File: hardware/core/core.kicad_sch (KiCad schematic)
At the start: 82 parts, among them J1 9V_IN, J2 MIDI IN, J3 MIDI OUT 1, J4 MIDI OUT 2, J5 MIDI OUT 3, J6 MIDI OUT 4, J7 LCD, J8 USB_C_Receptacle_USB2.0_16P, SW1 FS, SW10 BOOT, SW2 FS, SW3 FS, SW4 FS, SW5 FS, SW6 FS, SW7 FS, SW8 FS, SW9 RESET, U1 LM2596S-5, U2 6N137, U3 ESP32-S3-WROOM-1, U4 LD1117-3.3V-SOT223, U5 USBLC6-2SC6

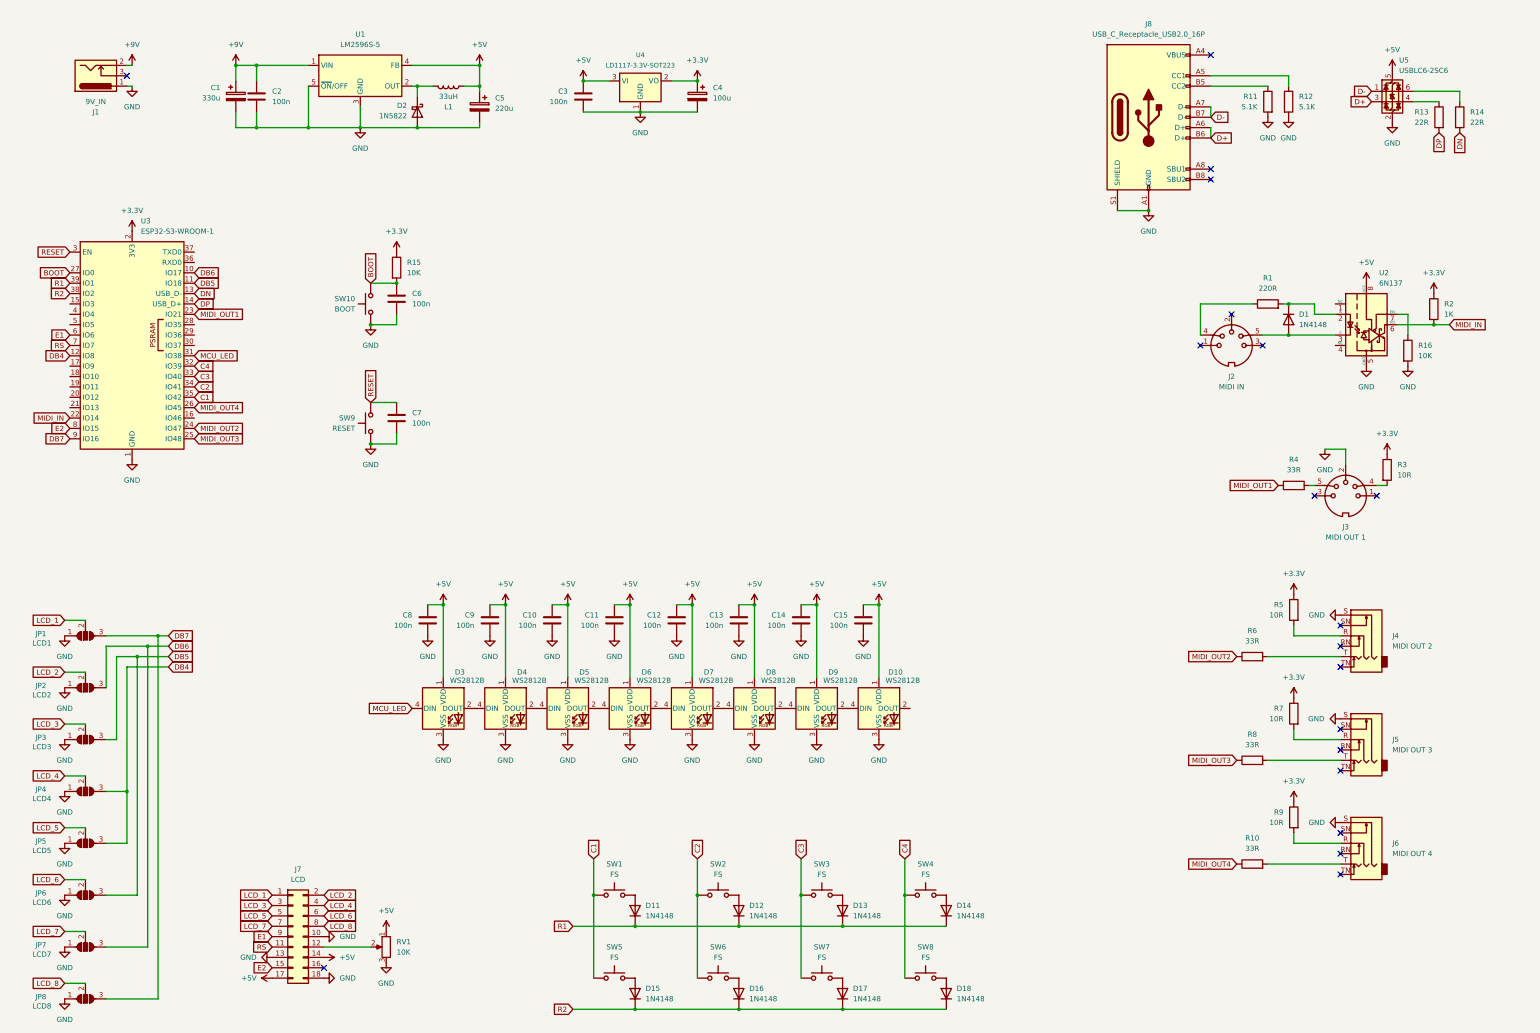
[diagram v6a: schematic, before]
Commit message: Add event system, switch matrix, MIDI outputs, and LED helpers
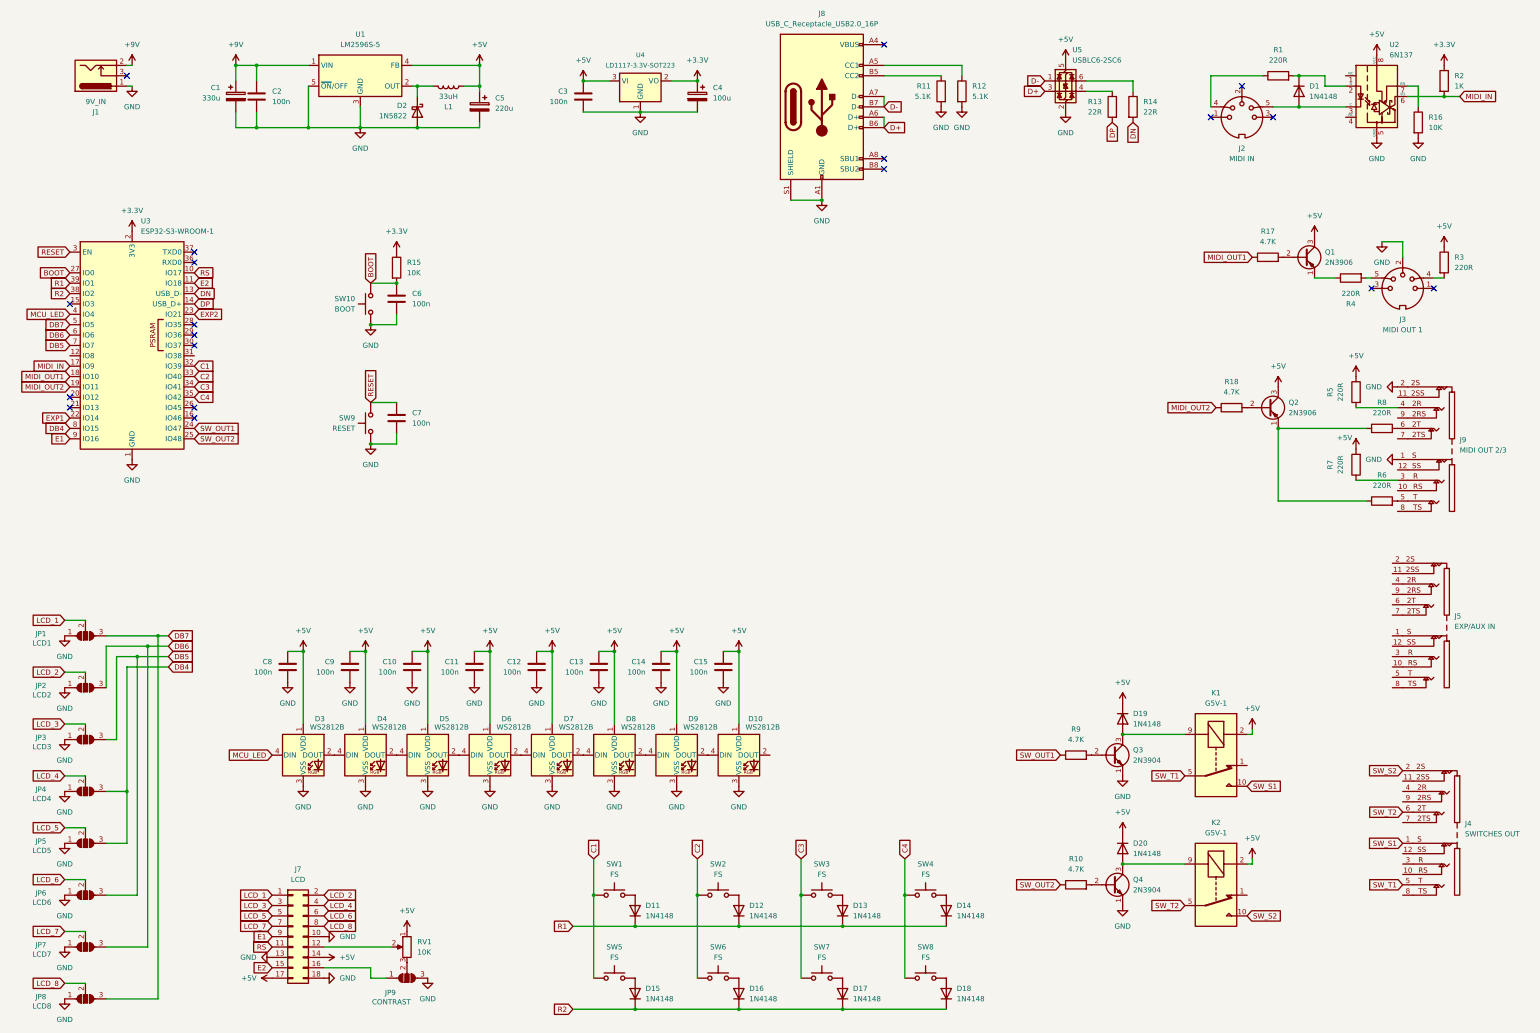
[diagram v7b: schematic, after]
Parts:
- removed J4: MIDI OUT 2, midilord:CK635-006, symbol Connector_Audio:AudioJack3_Switch
- removed J5: MIDI OUT 3, midilord:CK635-006, symbol Connector_Audio:AudioJack3_Switch
- removed J6: MIDI OUT 4, midilord:CK635-006, symbol Connector_Audio:AudioJack3_Switch
- added D19, D20: 1N4148, Diode_THT:D_T-1_P5.08mm_Horizontal, symbol Diode:1N4148
- added J4: SWITCHES OUT, midilord:CK635-037, symbol midilord:CK635-037
- added J5: EXP/AUX IN, midilord:CK635-037, symbol midilord:CK635-037
- added J9: MIDI OUT 2/3, midilord:CK635-037, symbol midilord:CK635-037
- added JP9: CONTRAST, Jumper:SolderJumper-3_P1.3mm_Open_RoundedPad1.0x1.5mm, symbol Jumper:SolderJumper_3_Open
- added K1, K2: G5V-1, Relay_THT:Relay_SPDT_Omron_G5V-1, symbol Relay:G5V-1
- added Q1, Q2: 2N3906, Package_TO_SOT_THT:TO-92_Inline_Wide, symbol Transistor_BJT:2N3906
- added Q3, Q4: 2N3904, Package_TO_SOT_THT:TO-92_Inline_Wide, symbol Transistor_BJT:2N3904
- added R17, R18: 4.7K, Resistor_THT:R_Axial_DIN0204_L3.6mm_D1.6mm_P7.62mm_Horizontal, symbol Device:R
- D11, D12, D13, D14, D15, D16, D17, D18: footprint Diode_THT:D_DO-35_SOD27_P7.62mm_Horizontal -> Diode_THT:D_T-1_P5.08mm_Horizontal
- R10: value 33R -> 4.7K
- R3, R5, R7: value 10R -> 220R
- R4, R6, R8: value 33R -> 220R
- R9: value 10R -> 4.7K
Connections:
- net +3.3V: no longer R3.1, R5.1, R7.1, R9.1
- net +5V: now also R3.1, R5.1, R7.2, D19.1 (K), D20.1 (K), K1.2, K2.2, Q1.3 (C), Q2.3 (C)
- net C1: now also U3.32 (IO39); no longer U3.35 (IO42)
- net C2: now also U3.33 (IO40); no longer U3.34 (IO41)
- net C3: now also U3.34 (IO41); no longer U3.33 (IO40)
- net C4: now also U3.35 (IO42); no longer U3.32 (IO39)
- net DB4: now also U3.8 (IO15); no longer U3.12 (IO8)
- net DB5: now also U3.7 (IO7); no longer U3.11 (IO18)
- net DB6: now also U3.6 (IO6); no longer U3.10 (IO17)
- net DB7: now also U3.5 (IO5); no longer U3.9 (IO16)
- net E1: now also U3.9 (IO16); no longer U3.6 (IO6)
- net E2: now also U3.11 (IO18); no longer U3.8 (IO15)
- net GND: now also J9.1 (S), J9.2 (2S), JP9.3 (B), Q3.1 (E), Q4.1 (E); no longer RV1.3
- net MCU_LED: now also U3.4 (IO4); no longer U3.31 (IO38)
- net MIDI_IN: now also U3.17 (IO9); no longer U3.22 (IO14)
- net MIDI_OUT1: now also U3.18 (IO10), R17.1; no longer R4.1, U3.23 (IO21)
- net MIDI_OUT2: now also U3.19 (IO11), R18.1; no longer R6.1, U3.24 (IO47)
- net RS: now also U3.10 (IO17); no longer U3.7 (IO7)
- net at R9.2: now also Q3.2 (B)
- net at R8.2: now also J9.6 (2T)
- net at R5.2: now also J9.4 (2R)
- net at R6.2: now also J9.5 (T)
- net at R10.2: now also Q4.2 (B)
- net at J7.16 (Pin_16): now also JP9.1 (A)
- net MIDI_OUT3: no longer names the net of R8.1
- net MIDI_OUT3: now also R6.1, Q2.1 (E); no longer U3.25 (IO48)
- net MIDI_OUT4: no longer names the net of U3.26 (IO45)
- net MIDI_OUT4: no longer R10.1
- new net: J9.3 (R), R7.1
- new net: D19.2 (A), K1.9, Q3.3 (C)
- new net: JP9.2 (C), RV1.3
- new net: D20.2 (A), K2.9, Q4.3 (C)
- new net: Q1.2 (B), R17.2
- new net: Q2.2 (B), R18.2
- new net: Q1.1 (E), R4.1
- new net EXP1: U3.22 (IO14)
- new net EXP2: U3.23 (IO21)
- new net SW_OUT1: R9.1, U3.24 (IO47)
- new net SW_OUT2: R10.1, U3.25 (IO48)
- new net SW_S1: J4.1 (S), K1.10
- new net SW_S2: J4.2 (2S), K2.10
- new net SW_T1: J4.5 (T), K1.5, K1.6
- new net SW_T2: J4.6 (2T), K2.5, K2.6
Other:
- moved on the sheet: C10, C11, C12, C13, C14, C15, C8, C9, D1, D10, D3, D4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

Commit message: Replace footswitch connector nets with aux/expression nets and renumber
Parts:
- added C16, C17: 10n, Capacitor_THT:C_Rect_L7.0mm_W2.5mm_P5.00mm, symbol Device:C
- added R19, R20, R21, R22: 2.2K, Resistor_THT:R_Axial_DIN0204_L3.6mm_D1.6mm_P7.62mm_Horizontal, symbol Device:R
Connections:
- net EXP1: now also C16.1, R22.1
- net EXP2: now also C17.1, R20.1
- net GND: now also J5.1 (S), J5.2 (2S), C16.2, C17.2
- net AUX1: now reaches U3.12 (IO8)
- net AUX1: now also R21.1
- net AUX2: now reaches U3.31 (IO38)
- net AUX2: now also R19.1
- net at J5.3 (R): now also R21.2
- net at J5.4 (2R): now also R19.2
- net at J5.5 (T): now also R22.2
- net at J5.6 (2T): now also R20.2
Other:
- moved on the sheet: D19, D20, J4, K1, K2, Q3, Q4, R10, R9
